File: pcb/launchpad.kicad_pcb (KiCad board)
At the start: 2 copper layers, 88.9 x 43.2 mm, 35 parts, among them J1 TYPE-C-31-M-12, J2 ICSP, SW0 CherryMX, SW1 CherryMX, SW2 CherryMX, SW3 CherryMX, SW4 CherryMX, SW5 CherryMX, SW6 CherryMX, U1 ATmega32U4-MUR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

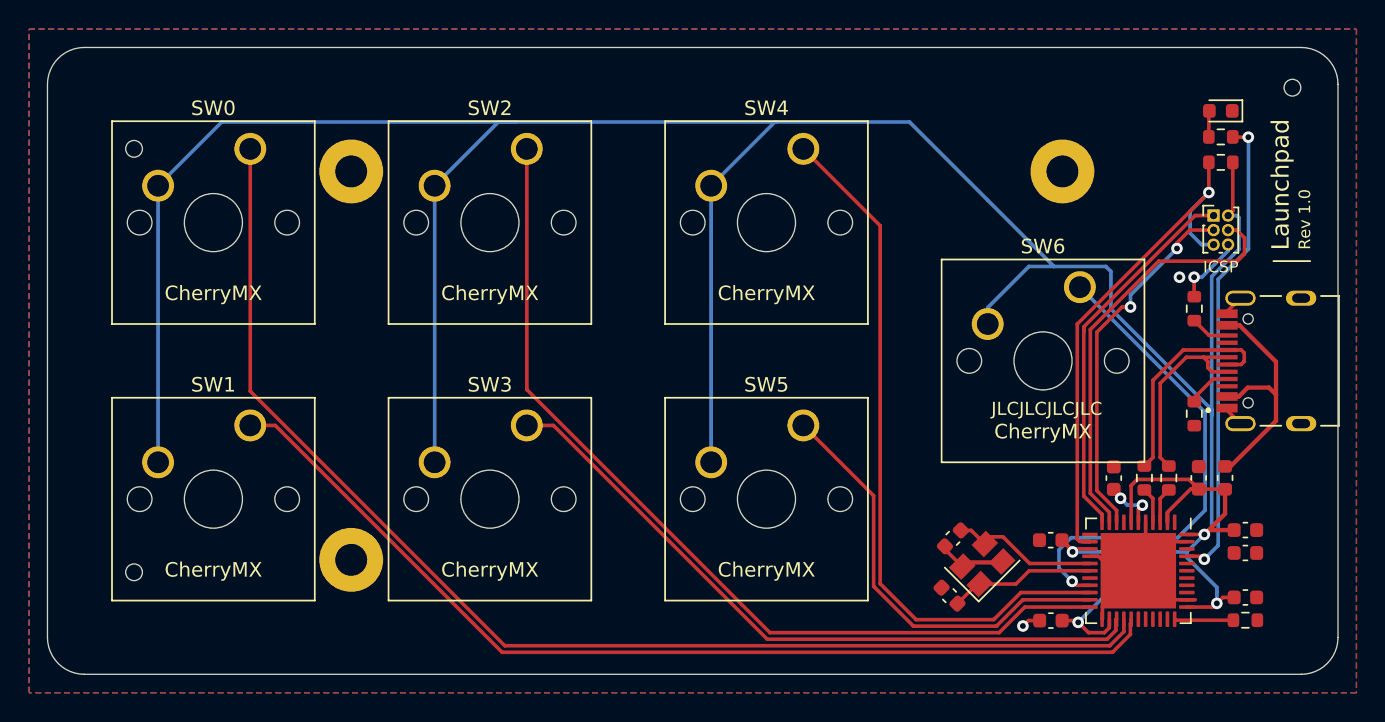
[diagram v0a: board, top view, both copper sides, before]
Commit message: So made the buttons active low. And found that I used the wrong ICSP header
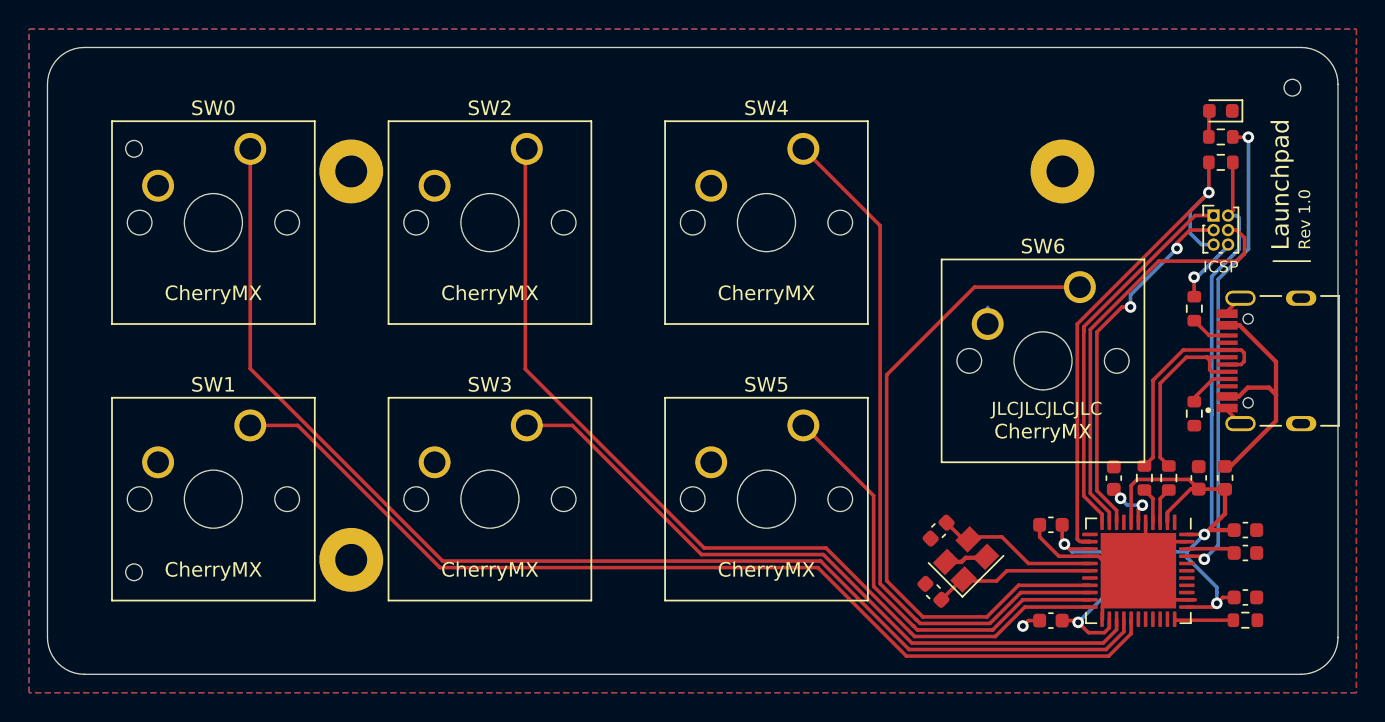
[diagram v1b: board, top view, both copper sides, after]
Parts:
- moved Y1 1.16 mm to (167.4, 84.8)
- moved C8 1.14 mm to (165.2, 87.0)
- moved C9 1.12 mm to (165.5, 82.8)
- moved C3 1.06 mm to (173.3, 82.4)
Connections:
- SW0 pad 2: +5V -> GND
- SW1 pad 2: +5V -> GND
- SW2 pad 2: +5V -> GND
- SW3 pad 2: +5V -> GND
- SW4 pad 2: +5V -> GND
- SW5 pad 2: +5V -> GND
- SW6 pad 2: +5V -> GND
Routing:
- net +5V: track 243.6 -> 82.4 mm
- net BTN6: track 34.0 -> 45.9 mm, vias 1 -> 0
- net GND: track 34.5 -> 38.4 mm, vias 3 -> 2
- net Net-(C1-Pad1): track 0.86 -> 4.25 mm
- net HSE_IN: track 10.1 -> 11.2 mm
- net HSE_OUT: track 10.2 -> 11.2 mm
- net BTN0: track 85.4 -> 84.7 mm

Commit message: Updated pinheader to appropiate size
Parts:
- J2: footprint Connector_PinHeader_1.00mm:PinHeader_2x03_P1.00mm_Vertical -> Connector_PinHeader_2.54mm:PinHeader_2x03_P2.54mm_Vertical
- moved R5 30.2 mm to (186.7, 85.9), turned to 0 degrees
- moved D2 25.4 mm to (187.4, 79.2), turned to 270 degrees
- moved R1 10.6 mm to (181.5, 67.5), turned to 90 degrees
- moved J2 3.28 mm to (184.1, 57.9)
- moved C3 0.13 mm to (173.3, 82.5)
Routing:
- net Net-(R5-Pad1): track 32.7 -> 3.75 mm, vias 2 -> 0
- net +5V: track 82.4 -> 97.9 mm, vias 4 -> 5
- net RESET: track 36.5 -> 31.1 mm
- net Net-(D2-Pad2): track 1.81 -> 6.92 mm
- net MISO: track 26.2 -> 28.6 mm
- net MOSI: track 29.1 -> 30.6 mm
- net GND: track 38.4 -> 37.1 mm, vias 2 -> 4
- net SCLK: track 25.3 -> 26.5 mm, vias 2 -> 0
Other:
- board text removed: "ICSP"

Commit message: Order is completed
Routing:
- net GND: track 37.1 -> 43.2 mm
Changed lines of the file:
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@@
     (thickness 1.6)
     (drawings 15)
-    (tracks 260)
+    (tracks 264)
     (zones 0)
     (modules 35)
@@
       (effects (font (size 1 1) (thickness 0.15)))
     )
-    (fp_text user %R (at 1.27 2.54 90) (layer F.Fab)
-      (effects (font (size 1 1) (thickness 0.15)))
-    )
     (fp_line (start 0 -1.27) (end 3.81 -1.27) (layer F.Fab) (width 0.1))
     (fp_line (start 3.81 -1.27) (end 3.81 6.35) (layer F.Fab) (width 0.1))
@@
     (fp_line (start 4.35 6.85) (end 4.35 -1.8) (layer F.CrtYd) (width 0.05))
     (fp_line (start 4.35 -1.8) (end -1.8 -1.8) (layer F.CrtYd) (width 0.05))
+    (fp_text user %R (at 1.27 2.54 90) (layer F.Fab)
+      (effects (font (size 1 1) (thickness 0.15)))
+    )
     (pad 6 thru_hole oval (at 2.54 5.08) (size 1.7 1.7) (drill 1) (layers *.Cu *.Mask)
       (net 41 GND))
@@
       (effects (font (size 1 1) (thickness 0.15)))
     )
-    (fp_text user %R (at 0 0 90) (layer F.Fab)
-      (effects (font (size 0.4 0.4) (thickness 0.06)))
-    )
     (fp_line (start 1.48 0.73) (end -1.48 0.73) (layer F.CrtYd) (width 0.05))
     (fp_line (start 1.48 -0.73) (end 1.48 0.73) (layer F.CrtYd) (width 0.05))
@@
     (fp_line (start -0.8 -0.4125) (end 0.8 -0.4125) (layer F.Fab) (width 0.1))
     (fp_line (start -0.8 0.4125) (end -0.8 -0.4125) (layer F.Fab) (width 0.1))
+    (fp_text user %R (at 0 0 90) (layer F.Fab)
+      (effects (font (size 0.4 0.4) (thickness 0.06)))
+    )
     (pad 2 smd roundrect (at 0.825 0 90) (size 0.8 0.95) (layers F.Cu F.Paste F.Mask) (roundrect_rratio 0.25)
       (net 6 RESET))
@@
   (segment (start 176.946802 89.84234) (end 175.85436 89.84234) (width 0.25) (layer F.Cu) (net 3))
   (via (at 183.8344 83.07768) (size 0.8) (drill 0.4) (layers F.Cu B.Cu) (net 3))
-  (segment (start 182.62594 83.07768) (end 183.8344 83.07768) (width 0.25) (layer F.Cu) (net 3))
   (segment (start 175.14316 89.13114) (end 179.9971 84.2772) (width 0.25) (layer B.Cu) (net 3))
   (segment (start 183.85218 83.0599) (end 183.8344 83.07768) (width 0.25) (layer F.Cu) (net 3))
@@
   (segment (start 181.28844 81.55076) (end 182.88508 79.95412) (width 0.25) (layer F.Cu) (net 3))
   (segment (start 185.58214 83.07768) (end 185.88452 82.7753) (width 0.25) (layer F.Cu) (net 3))
-  (segment (start 184.13678 82.7753) (end 183.8344 83.07768) (width 0.3) (layer F.Cu) (net 3))
-  (segment (start 185.88452 82.7753) (end 184.13678 82.7753) (width 0.3) (layer F.Cu) (net 3))
-  (segment (start 185.26252 81.64956) (end 184.13678 82.7753) (width 0.3) (layer F.Cu) (net 3))
-  (segment (start 185.26252 79.96662) (end 185.26252 81.64956) (width 0.3) (layer F.Cu) (net 3))
   (segment (start 184.0249 88.07768) (end 184.64022 87.46236) (width 0.25) (layer F.Cu) (net 3))
   (segment (start 182.62594 88.07768) (end 184.0249 88.07768) (width 0.25) (layer F.Cu) (net 3))
@@
   (via (at 174.04334 83.77936) (size 0.8) (drill 0.4) (layers F.Cu B.Cu) (net 3))
   (segment (start 183.8344 86.65654) (end 184.64022 87.46236) (width 0.25) (layer B.Cu) (net 3))
-  (segment (start 183.8344 83.07768) (end 183.8344 86.65654) (width 0.25) (layer B.Cu) (net 3))
   (segment (start 181.19662 83.07768) (end 179.9971 84.2772) (width 0.25) (layer B.Cu) (net 3))
-  (segment (start 183.8344 83.07768) (end 181.19662 83.07768) (width 0.25) (layer B.Cu) (net 3))
   (segment (start 174.34166 84.07768) (end 174.04334 83.77936) (width 0.25) (layer F.Cu) (net 3))
   (segment (start 175.95094 84.07768) (end 174.34166 84.07768) (width 0.25) (layer F.Cu) (net 3))
@@
   (segment (start 178.116935 68.294955) (end 176.45169 69.9602) (width 0.25) (layer B.Cu) (net 3))
   (segment (start 181.33709 65.0748) (end 178.116935 68.294955) (width 0.25) (layer B.Cu) (net 3))
+  (segment (start 183.8344 83.07768) (end 183.8344 86.65654) (width 0.25) (layer B.Cu) (net 3))
+  (segment (start 183.8344 83.07768) (end 181.19662 83.07768) (width 0.25) (layer B.Cu) (net 3))
+  (segment (start 185.26252 79.96662) (end 185.26252 81.64956) (width 0.3) (layer F.Cu) (net 3))
+  (segment (start 182.62594 83.07768) (end 183.8344 83.07768) (width 0.25) (layer F.Cu) (net 3))
+  (segment (start 184.13678 82.7753) (end 183.8344 83.07768) (width 0.3) (layer F.Cu) (net 3))
+  (segment (start 185.88452 82.7753) (end 184.13678 82.7753) (width 0.3) (layer F.Cu) (net 3))
+  (segment (start 185.26252 81.64956) (end 184.13678 82.7753) (width 0.3) (layer F.Cu) (net 3))
   (segment (start 167.351825 86.28126) (end 167.242243 86.171678) (width 0.25) (layer F.Cu) (net 4))
   (segment (start 169.52468 86.28126) (end 167.351825 86.28126) (width 0.25) (layer F.Cu) (net 4))
@@
   (segment (start 182.62594 87.57768) (end 181.28844 87.57768) (width 0.25) (layer F.Cu) (net 41))
   (segment (start 176.81345 88.05267) (end 179.28844 85.57768) (width 0.25) (layer F.Cu) (net 41))
-  (segment (start 176.81345 88.89017) (end 176.81345 88.05267) (width 0.25) (layer F.Cu) (net 41))
-  (segment (start 176.78844 88.91518) (end 176.81345 88.89017) (width 0.25) (layer F.Cu) (net 41))
   (segment (start 182.62594 87.57768) (end 183.211462 87.57768) (width 0.25) (layer F.Cu) (net 41))
   (segment (start 183.12638 66.68312) (end 183.14162 66.69836) (width 0.25) (layer F.Cu) (net 41))
@@
   (segment (start 173.28972 84.57768) (end 172.48826 83.77622) (width 0.25) (layer F.Cu) (net 41))
   (via (at 177.673 74.49312) (size 0.8) (drill 0.4) (layers F.Cu B.Cu) (net 41))
-  (via (at 177.673 73.28916) (size 0.8) (drill 0.4) (layers F.Cu B.Cu) (net 41))
   (via (at 186.45632 81.28762) (size 0.8) (drill 0.4) (layers F.Cu B.Cu) (net 41))
   (segment (start 186.45632 79.30482) (end 187.36952 78.39162) (width 0.25) (layer F.Cu) (net 41))
   (segment (start 186.45632 81.28762) (end 186.45632 79.30482) (width 0.25) (layer F.Cu) (net 41))
+  (segment (start 182.62594 87.57768) (end 183.3692 87.57768) (width 0.25) (layer F.Cu) (net 41))
+  (via (at 184.64022 86.29142) (size 0.8) (drill 0.4) (layers F.Cu B.Cu) (net 41))
+  (segment (start 184.65546 86.29142) (end 184.67578 86.29142) (width 0.25) (layer F.Cu) (net 41))
+  (segment (start 183.3692 87.57768) (end 184.65546 86.29142) (width 0.25) (layer F.Cu) (net 41))
+  (segment (start 179.28844 85.825702) (end 179.28844 85.57768) (width 0.25) (layer F.Cu) (net 41))
+  (segment (start 176.78844 88.325702) (end 179.28844 85.825702) (width 0.25) (layer F.Cu) (net 41))
+  (segment (start 176.78844 88.91518) (end 176.78844 88.325702) (width 0.25) (layer F.Cu) (net 41))
   (segment (start 186.253998 68.67) (end 188.77026 71.186262) (width 0.3) (layer F.Cu) (net 42))
   (segment (start 185.405 68.67) (end 186.253998 68.67) (width 0.3) (layer F.Cu) (net 42))
